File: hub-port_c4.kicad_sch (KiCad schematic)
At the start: 24 parts, among them J6 USB-C USB2.0, Q6 2N7002, U15 TPS2553DBVR, U19 USBLC6-2SC6, U21 TUSB320LAIRWBR, U36 SN74LVC1G04DBVR, U38 SN74LVC1G08DBVR, U40 SN74LVC1G04DBVR

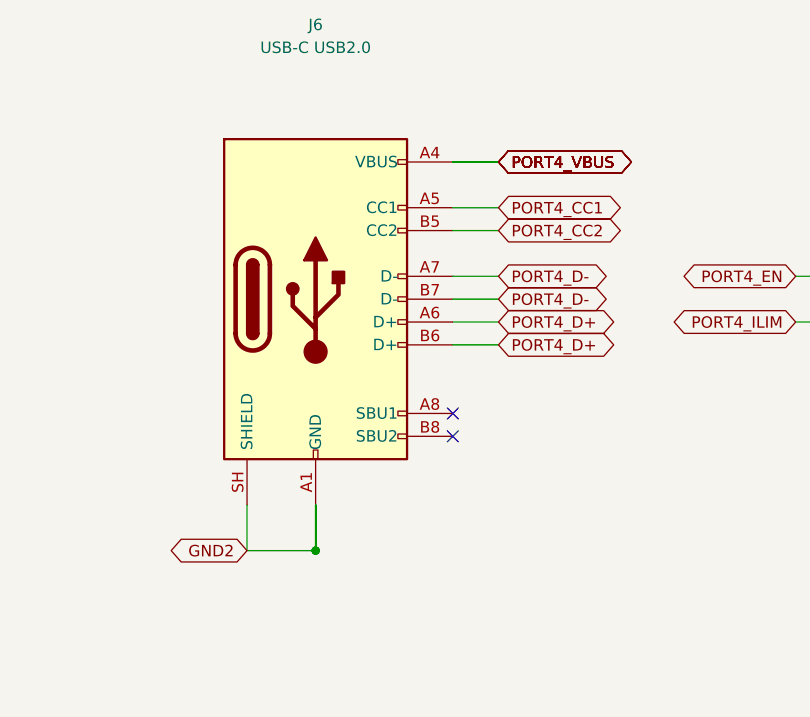
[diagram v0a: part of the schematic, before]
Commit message: feat(revc): assign exact BOM and verified local land patterns
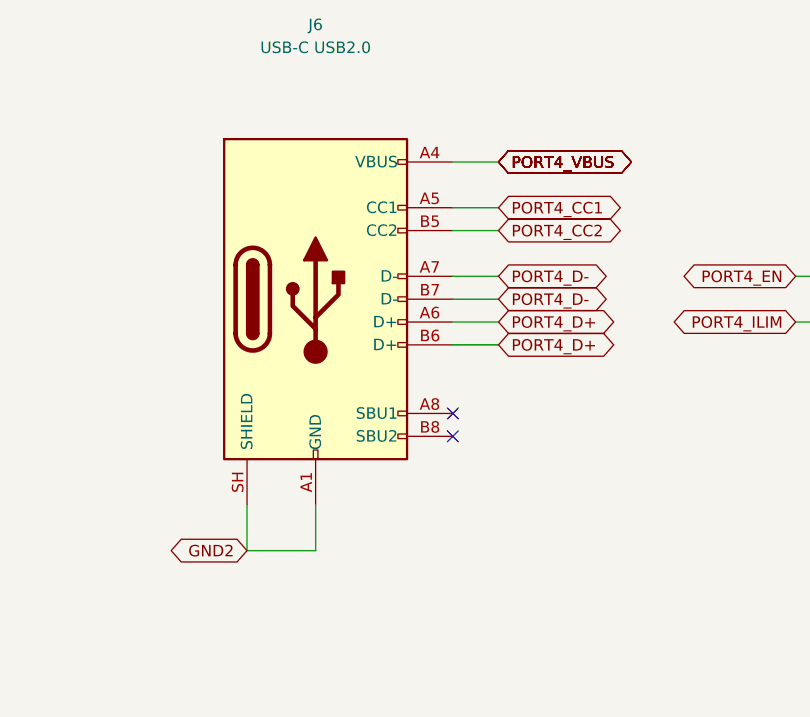
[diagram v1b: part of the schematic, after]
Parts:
- C103, C104, C105, C106, C55, C57: footprint (none) -> hub-lib:C_0402_1005Metric; LCSC (none) -> C77020; MPN (none) -> GRM155R71H104KE14D; Manufacturer (none) -> Murata Manufacturing; Ratings (none) -> 50V X7R 10%
- C56: footprint (none) -> hub-lib:C_0805_2012Metric; LCSC (none) -> C84416; MPN (none) -> GRM21BR61E106KA73L; Manufacturer (none) -> Murata Manufacturing; Ratings (none) -> 25V X5R 10%
- D13: footprint Diode_SMD:D_SOD-523 -> hub-lib:D_SOD-523; LCSC (none) -> C19950551; Ratings (none) -> See exact manufacturer datasheet
- J6: footprint Connector_USB:USB_C_Receptacle_HRO_TYPE-C-31-M-12 -> hub-lib:USB_C_Receptacle_HRO_TYPE-C-31-M-12; LCSC (none) -> C165948; Ratings (none) -> See exact manufacturer datasheet
- Q6: footprint Package_TO_SOT_SMD:SOT-23 -> hub-lib:SOT-23; LCSC (none) -> C65189; Ratings (none) -> See exact manufacturer datasheet
- R104, R50: footprint (none) -> hub-lib:R_0402_1005Metric; LCSC (none) -> C192169; MPN (none) -> ERJ2RKF1003X; Manufacturer (none) -> Panasonic Industry; Ratings (none) -> 1%, 0.1W, 50V
- R120, R76: footprint (none) -> hub-lib:R_0402_1005Metric; LCSC (none) -> C191123; MPN (none) -> ERJ2RKF1002X; Manufacturer (none) -> Panasonic Industry; Ratings (none) -> 1%, 0.1W, 50V
- R44: footprint (none) -> hub-lib:R_0402_1005Metric; LCSC (none) -> C416544; MPN (none) -> ERJ2RKF4642X; Manufacturer (none) -> Panasonic Industry; Ratings (none) -> 1%, 0.1W, 50V
- R75: footprint (none) -> hub-lib:R_0402_1005Metric; LCSC (none) -> C400631; MPN (none) -> ERJ2RKF4701X; Manufacturer (none) -> Panasonic Industry; Ratings (none) -> 1%, 0.1W, 50V
- R77: footprint (none) -> hub-lib:R_0402_1005Metric; LCSC (none) -> C2085054; MPN (none) -> ERJ2RKF9093X; Manufacturer (none) -> Panasonic Industry; Ratings (none) -> 1%, 0.1W, 50V
- R82: footprint (none) -> hub-lib:R_0805_2012Metric; LCSC (none) -> C193990; MPN (none) -> ERJ6ENF1000V; Manufacturer (none) -> Panasonic Industry; Ratings (none) -> 100R 1%, 0.125W; 0.14mJ maximum discharge pulse
- U15: footprint (none) -> hub-lib:SOT-23-6; LCSC (none) -> C55266; Ratings (none) -> See exact manufacturer datasheet
- U19: footprint Package_TO_SOT_SMD:SOT-23-6 -> hub-lib:SOT-23-6; LCSC (none) -> C7519; Ratings (none) -> See exact manufacturer datasheet
- U21: footprint (none) -> hub-lib:Texas_X2QFN-12_1.6x1.6mm_P0.4mm; LCSC (none) -> C132554; Ratings (none) -> See exact manufacturer datasheet
- U36, U40: footprint (none) -> hub-lib:SOT-23-5; LCSC (none) -> C7827; Ratings (none) -> See exact manufacturer datasheet
- U38: footprint (none) -> hub-lib:SOT-23-5; LCSC (none) -> C7666; Ratings (none) -> See exact manufacturer datasheet

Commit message: feat(revc): place synchronized unrouted board and correct bus startup
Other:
- note added: "Attach detection: DFP, default Rp, no VCONN"
- note added: "Attachment AND hub permission controls VBUS"
- note added: "Detach discharge, including total board power loss"
- note added: "Port 4: USB-C, USB 2.0 and ESD"
- note added: "USB 2.0 / 480 Mbps | Rev C electrical design | Placement and routing review pending"
- note removed: "Rev C | all routing reserved for Alex | electrical draft under review"
- moved on the sheet: C103, C104, C105, C106, C55, C56, C57, D13, J6, Q6, R104, R120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

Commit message: feat(revc): finish verified TI hub routing handoff
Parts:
- R82: Ratings 100R 1%, 0.125W; 0.14mJ maximum discharge pulse -> 100R 1%, 0.125W; 0.20mJ maximum design discharge pulse
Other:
- note added: "USB 2.0 / 480 Mbps | Rev C electrical design | Placed PCB; all routing by Alex; hardware tests pending"
- note removed: "USB 2.0 / 480 Mbps | Rev C electrical design | Placement and routing review pending"
- moved on the sheet: D13, Q6, R120, R82
